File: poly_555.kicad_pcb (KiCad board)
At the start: 2 copper layers, 129 parts, among them U1 LM386, U10 555, U11 555, U12 555, U13 555, U14 555, U2 555, U3 555, U4 555, U5 555, U6 555, U7 555, U8 555, U9 555

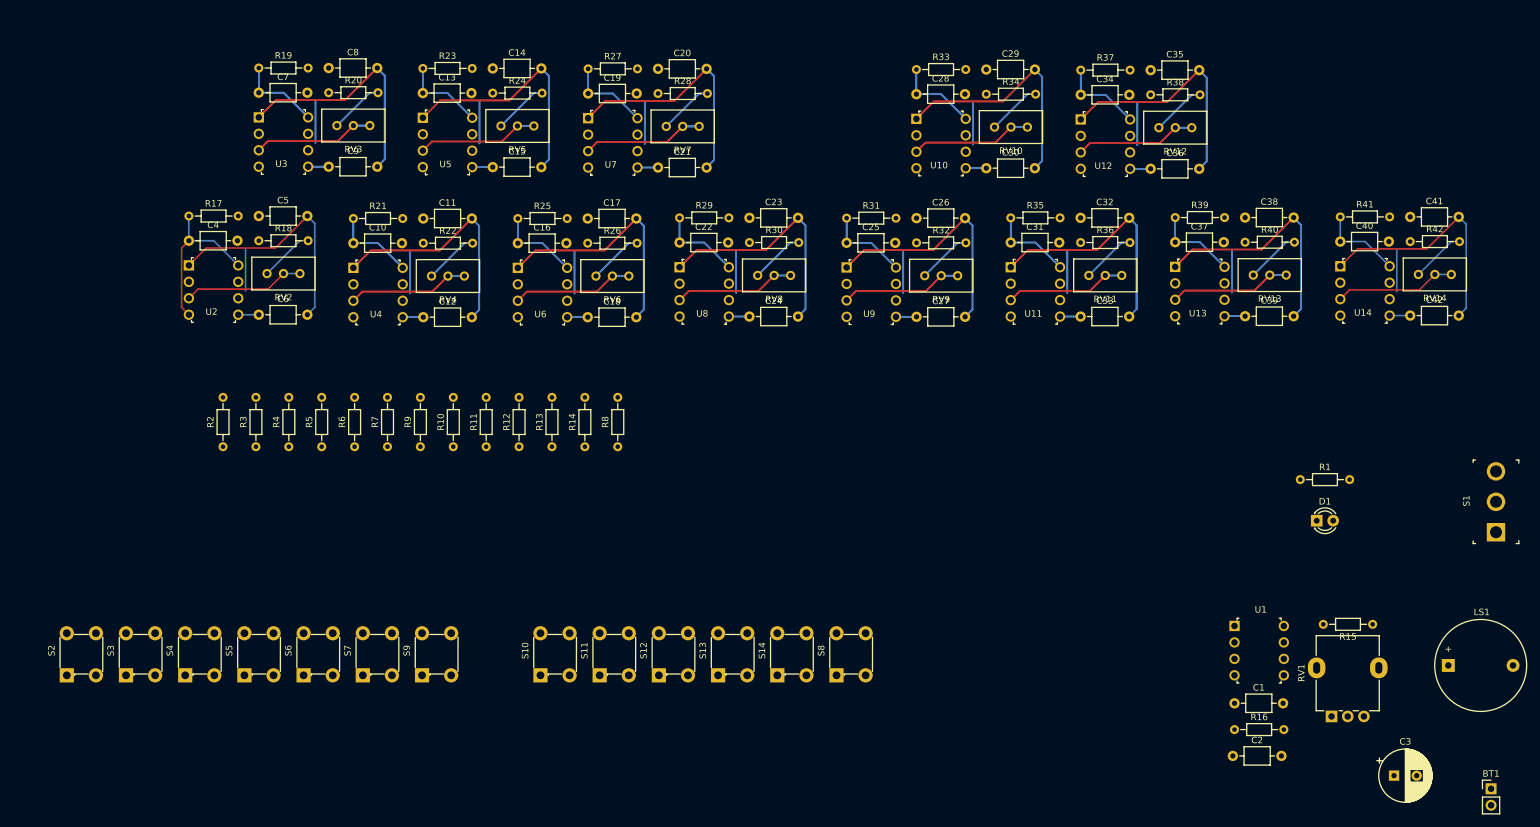
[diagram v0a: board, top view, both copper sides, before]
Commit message: Fixed button layout
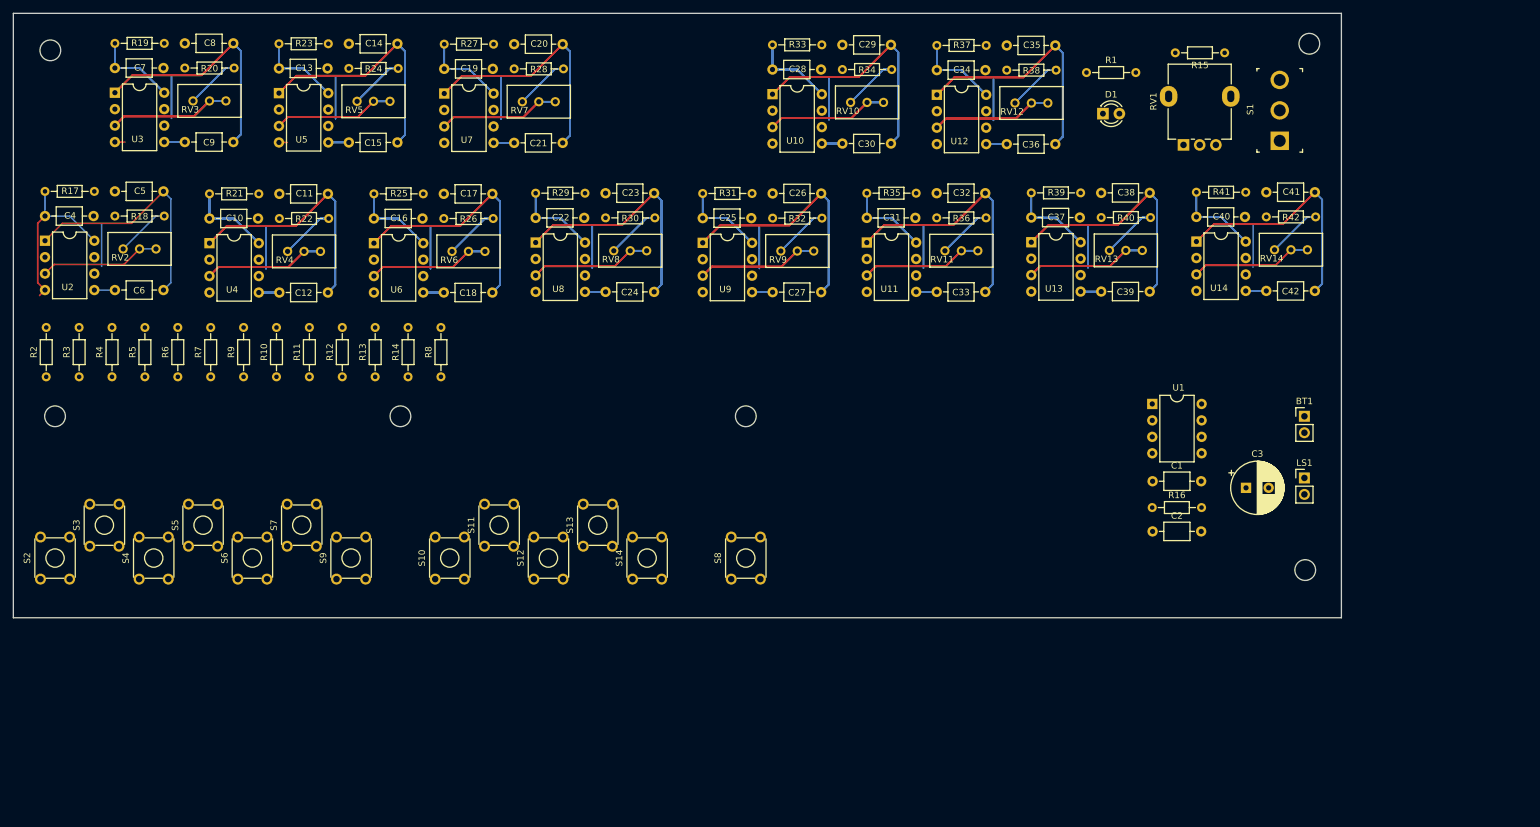
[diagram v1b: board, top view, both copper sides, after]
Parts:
- added ?: , , F.Cu at (120.4, 121.8)
- added REF**: MountingHole_3.2mm_M3, MountingHole:MountingHole_3.2mm_M3, F.Cu at (216.7, 114.6)
- added REF**: MountingHole_3.2mm_M3, MountingHole:MountingHole_3.2mm_M3, F.Cu at (217.3, 33.3)
- added REF**: MountingHole_3.2mm_M3, MountingHole:MountingHole_3.2mm_M3, F.Cu at (22.9, 34.3)
- added REF**: MountingHole_3.2mm_M3, MountingHole:MountingHole_3.2mm_M3, F.Cu at (76.9, 90.8)
- added REF**: MountingHole_3.2mm_M3, MountingHole:MountingHole_3.2mm_M3, F.Cu at (130.3, 90.8)
- added REF**: MountingHole_3.2mm_M3, MountingHole:MountingHole_3.2mm_M3, F.Cu at (23.6, 90.8)
- LS1: footprint Buzzer_Beeper:Buzzer_D14mm_H7mm_P10mm -> Connector_PinHeader_2.54mm:PinHeader_1x02_P2.54mm_Vertical
- S10, S11, S12, S13, S14, S2, S3, S4, S5, S6, S7, S8, S9: footprint digikey-footprints:Switch_Tactile_THT_6x6mm -> Button_Switch_THT:SW_TH_Tactile_Omron_B3F-10xx
- U1, U10, U11, U12, U13, U14, U2, U3, U4, U5, U6, U7, U8, U9: footprint digikey-footprints:DIP-8_W7.62mm -> Package_DIP:DIP-8_W7.62mm
- moved R15 91.2 mm to (204.2, 34.7)
- moved RV1 91.2 mm to (197.9, 48.9)
- moved D1 71.0 mm to (185.4, 44.1)
- moved R1 71.0 mm to (182.9, 37.7)
- moved S1 69.1 mm to (212.7, 48.3)
- moved BT1 64.4 mm to (216.5, 90.8)
- moved C3 50.0 mm to (207.5, 101.9)
- moved C2 36.8 mm to (193.1, 108.6)
- moved R16 36.6 mm to (193.0, 104.9)
- moved U1 36.6 mm to (193.0, 88.9)
- moved C1 36.5 mm to (193.1, 100.8)
- moved LS1 36.5 mm to (216.5, 100.3)
- moved R10 29.4 mm to (57.8, 84.7)
- moved R12 29.4 mm to (67.9, 84.7)
- moved R7 29.4 mm to (47.6, 84.7)
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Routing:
- net GND: track 903.4 -> 1355.0 mm
- net /sheet5EF60553/Out: track 37.4 -> 56.2 mm
- net /sheet5EF60554/Out: track 37.4 -> 56.2 mm
- net /sheet5EF60555/Out: track 37.4 -> 56.2 mm
- net /sheet5EF60550/Out: track 37.4 -> 56.2 mm
- net /sheet5EF27E47/Out: track 37.4 -> 56.2 mm
- net /sheet5EF259DC/Out: track 37.4 -> 56.2 mm
- net /sheet5EF7A07A/Out: track 18.7 -> 37.4 mm
- net /sheet5EF60552/Out: track 37.4 -> 56.2 mm
- net /sheet5EF17814/Out: track 37.4 -> 56.2 mm
- net /sheet5EF2B20E/Out: track 37.4 -> 56.2 mm
- net /sheet5EF2302B/Out: track 37.4 -> 56.2 mm
- net /sheet5EF60551/Out: track 37.4 -> 56.2 mm
- net /sheet5EF17814/9v: track 26.0 -> 40.6 mm
- net /sheet5EF259DC/9v: track 26.0 -> 40.3 mm
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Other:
- board outline added: 205.1 x 93.3 mm

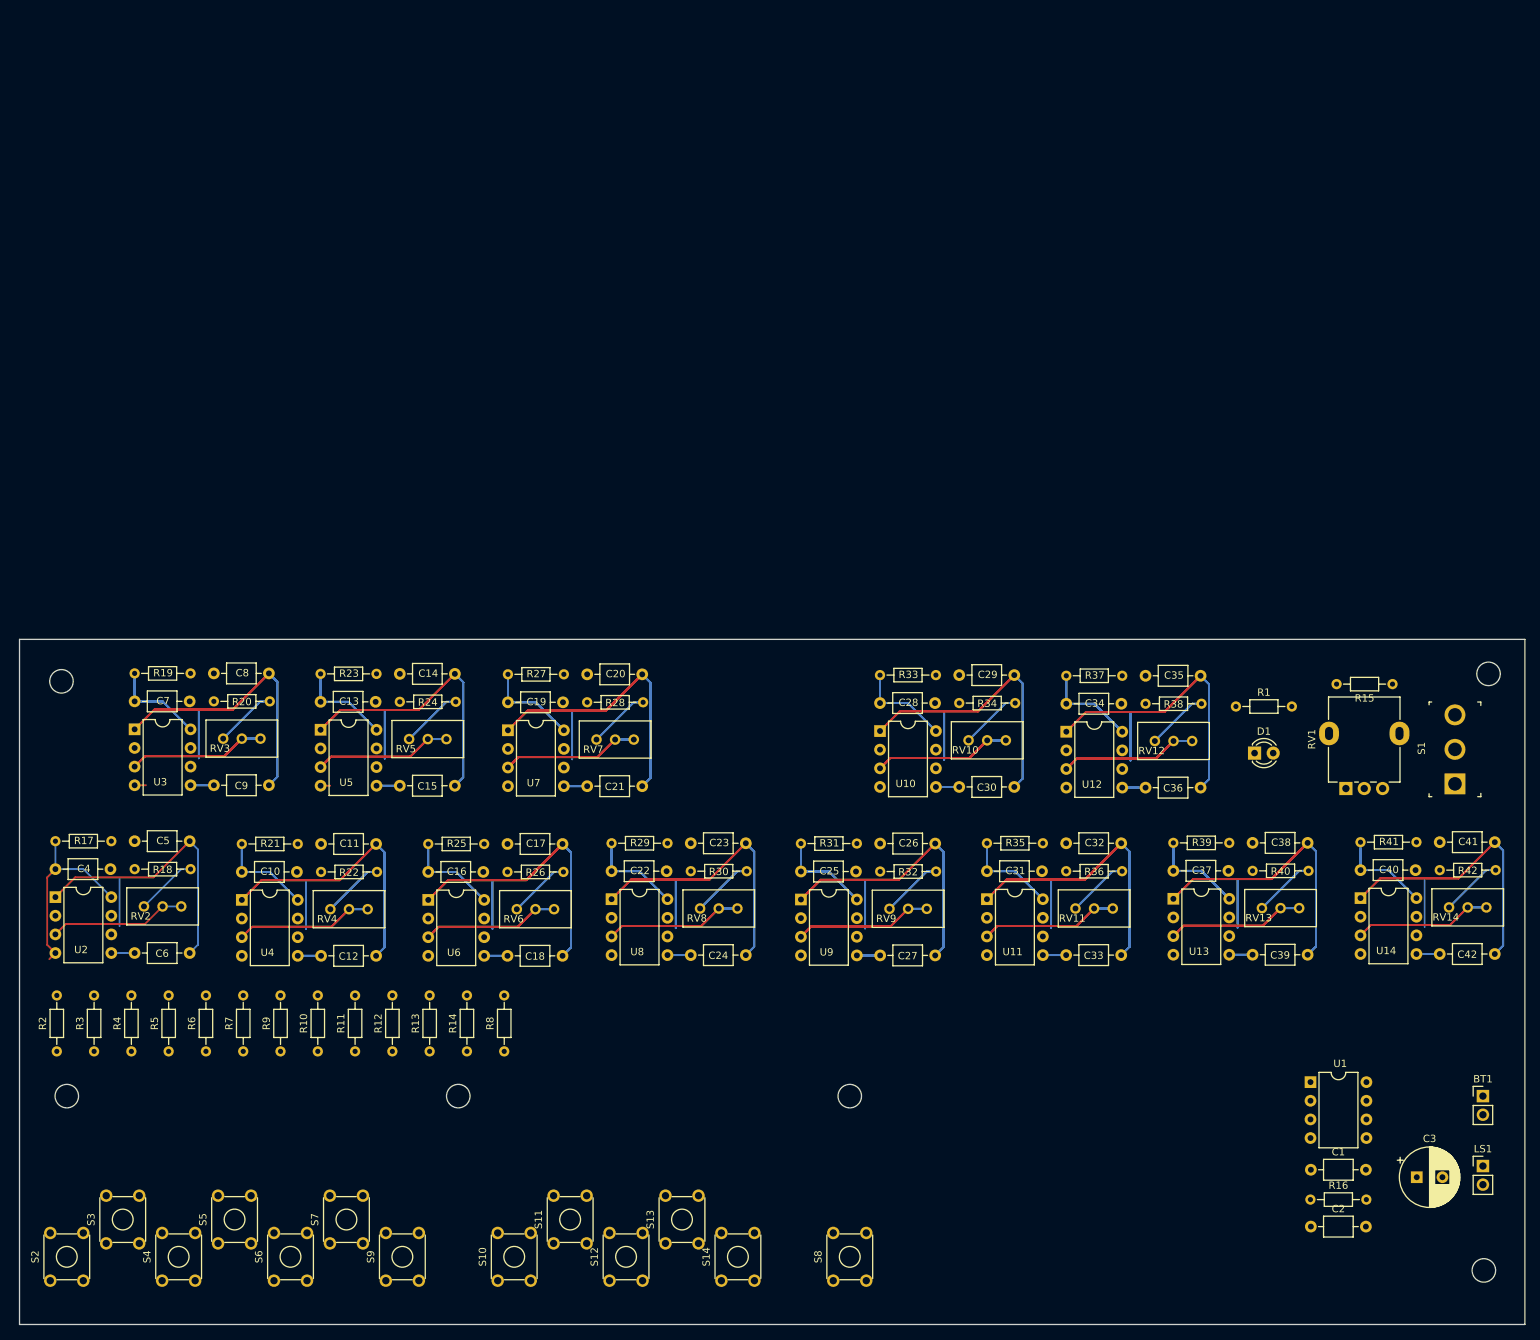
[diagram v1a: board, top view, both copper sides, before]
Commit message: Portrait layout, LEDs
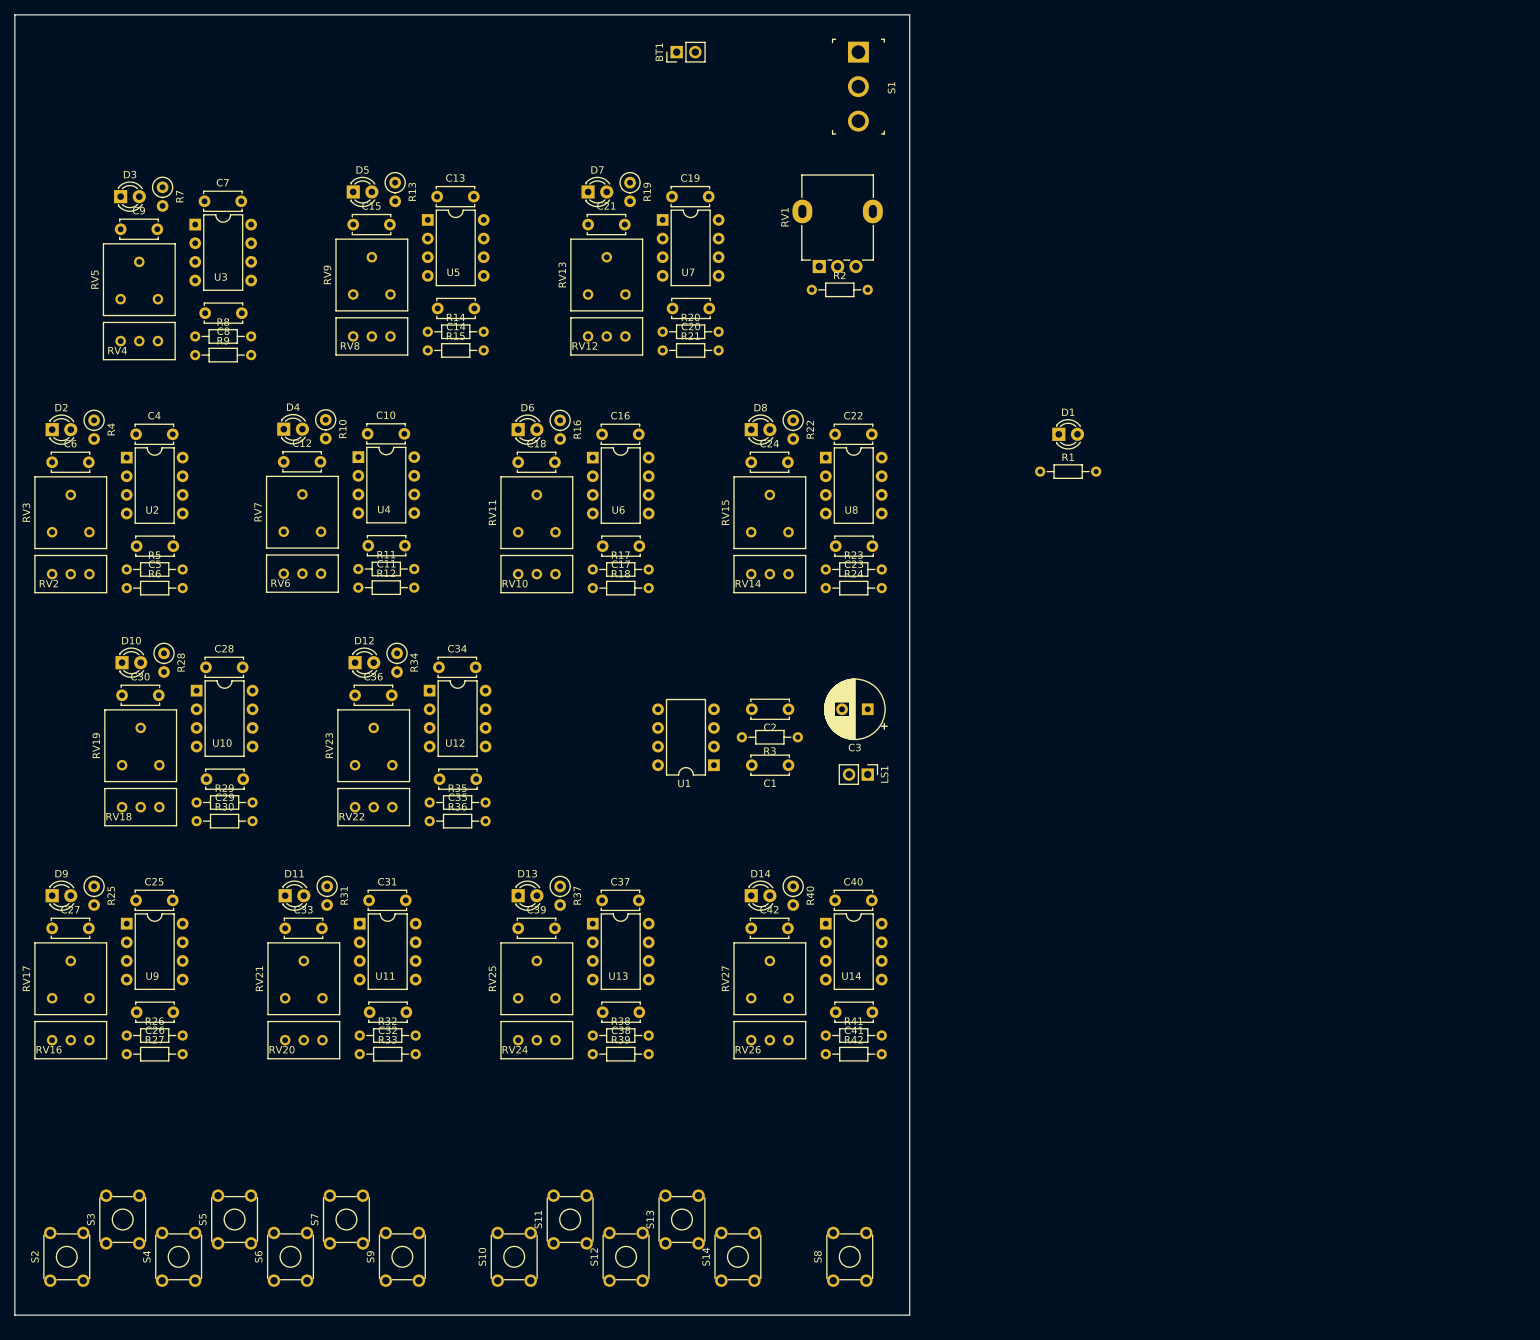
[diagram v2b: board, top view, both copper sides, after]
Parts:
- removed ?: , 
- removed REF** (x6): MountingHole_3.2mm_M3, MountingHole:MountingHole_3.2mm_M3
- added D10: LED, LED_THT:LED_D3.0mm, F.Cu at (31.1, 31.8)
- added D11: LED, LED_THT:LED_D3.0mm, F.Cu at (53.3, 63.5)
- added D12: LED, LED_THT:LED_D3.0mm, F.Cu at (62.9, 31.8)
- added D13: LED, LED_THT:LED_D3.0mm, F.Cu at (85.1, 63.5)
- added D14: LED, LED_THT:LED_D3.0mm, F.Cu at (116.8, 63.5)
- added D2: LED, LED_THT:LED_D3.0mm, F.Cu at (21.6, 0.00)
- added D3: LED, LED_THT:LED_D3.0mm, F.Cu at (30.9, -31.8)
- added D4: LED, LED_THT:LED_D3.0mm, F.Cu at (53.1, -0.06)
- added D5: LED, LED_THT:LED_D3.0mm, F.Cu at (62.6, -32.4)
- added D6: LED, LED_THT:LED_D3.0mm, F.Cu at (85.1, 0.00)
- added D7: LED, LED_THT:LED_D3.0mm, F.Cu at (94.6, -32.4)
- added D8: LED, LED_THT:LED_D3.0mm, F.Cu at (116.8, 0.00)
- added D9: LED, LED_THT:LED_D3.0mm, F.Cu at (21.6, 63.5)
- added RV15: R_POT_TRIM_US, Potentiometer_THT:Potentiometer_Bourns_3386F_Vertical, F.Cu at (121.9, 14.0)
- added RV16: R_POT_TRIM_US, Potentiometer_THT:Potentiometer_Bourns_3296W_Vertical, F.Cu at (21.6, 83.2)
- added RV17: R_POT_TRIM_US, Potentiometer_THT:Potentiometer_Bourns_3386F_Vertical, F.Cu at (26.7, 77.5)
- added RV18: R_POT_TRIM_US, Potentiometer_THT:Potentiometer_Bourns_3296W_Vertical, F.Cu at (31.1, 51.4)
- added RV19: R_POT_TRIM_US, Potentiometer_THT:Potentiometer_Bourns_3386F_Vertical, F.Cu at (36.2, 45.7)
- added RV20: R_POT_TRIM_US, Potentiometer_THT:Potentiometer_Bourns_3296W_Vertical, F.Cu at (53.3, 83.2)
- added RV21: R_POT_TRIM_US, Potentiometer_THT:Potentiometer_Bourns_3386F_Vertical, F.Cu at (58.4, 77.5)
- added RV22: R_POT_TRIM_US, Potentiometer_THT:Potentiometer_Bourns_3296W_Vertical, F.Cu at (62.9, 51.4)
- added RV23: R_POT_TRIM_US, Potentiometer_THT:Potentiometer_Bourns_3386F_Vertical, F.Cu at (67.9, 45.7)
- added RV24: R_POT_TRIM_US, Potentiometer_THT:Potentiometer_Bourns_3296W_Vertical, F.Cu at (85.1, 83.2)
- added RV25: R_POT_TRIM_US, Potentiometer_THT:Potentiometer_Bourns_3386F_Vertical, F.Cu at (90.2, 77.5)
- added RV26: R_POT_TRIM_US, Potentiometer_THT:Potentiometer_Bourns_3296W_Vertical, F.Cu at (116.8, 83.2)
- added RV27: R_POT_TRIM_US, Potentiometer_THT:Potentiometer_Bourns_3386F_Vertical, F.Cu at (121.9, 77.5)
- C1, C10, C11, C12, C13, C14, C15, C16, C17, C18, C19, C2, C20, C21, C22, C23, C24, C25, C26, C27, C28, C29, C30, C31, C32, C33, C34, C35, C36, C37, C38, C39, C4, C40, C41, C42, C5, C6, C7, C8, C9: footprint Capacitor_THT:C_Axial_L3.8mm_D2.6mm_P7.50mm_Horizontal -> Capacitor_THT:C_Disc_D5.0mm_W2.5mm_P5.00mm
- R10, R13, R4, R7: value 10k -> 330; footprint Resistor_THT:R_Axial_DIN0204_L3.6mm_D1.6mm_P7.62mm_Horizontal -> Resistor_THT:R_Axial_DIN0207_L6.3mm_D2.5mm_P2.54mm_Vertical
- R11, R14, R5, R8: value 10k -> 100k
- R15: value 10 -> 10k
- R16: value 10 -> 330; footprint Resistor_THT:R_Axial_DIN0204_L3.6mm_D1.6mm_P7.62mm_Horizontal -> Resistor_THT:R_Axial_DIN0207_L6.3mm_D2.5mm_P2.54mm_Vertical
- R18, R21, R24, R27, R30, R33, R36, R39, R42: value 100k -> 10k
- R19, R22, R25, R28, R31, R34, R37, R40: value 100k -> 330; footprint Resistor_THT:R_Axial_DIN0204_L3.6mm_D1.6mm_P7.62mm_Horizontal -> Resistor_THT:R_Axial_DIN0207_L6.3mm_D2.5mm_P2.54mm_Vertical
- R2, R3: value 10k -> 10
- RV11, RV13, RV3, RV5, RV7, RV9: footprint Potentiometer_THT:Potentiometer_Bourns_3296W_Vertical -> Potentiometer_THT:Potentiometer_Bourns_3386F_Vertical
- moved BT1 179.7 mm to (106.7, -51.4), turned to 90 degrees
- moved R16 147.4 mm to (90.8, -1.27), turned to 270 degrees
- moved R2 146.1 mm to (125.1, -19.1), turned to 0 degrees
- moved R15 139.1 mm to (72.8, -10.8), turned to 0 degrees
- moved S1 128.6 mm to (131.4, -51.4), turned to 270 degrees
- moved RV13 120.5 mm to (99.7, -18.4), turned to 90 degrees
- moved R13 118.5 mm to (68.3, -33.7), turned to 270 degrees
- moved R7 118.2 mm to (36.6, -33.0), turned to 270 degrees
- moved C30 114.7 mm to (31.1, 36.2)
- moved C27 112.9 mm to (21.6, 67.9)
- moved C36 108.4 mm to (62.9, 36.2)
- moved RV9 107.8 mm to (67.7, -18.4), turned to 90 degrees
- moved C33 106.5 mm to (53.3, 67.9)
- moved R8 106.1 mm to (41.1, -12.7), turned to 0 degrees
- moved RV14 105.4 mm to (116.8, 19.7)
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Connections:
- R10 pad 1: Net-(R10-Pad1) -> /sheet5EF2302B/9v
- R10 pad 2: /sheet5EF60551/Out -> Net-(D4-Pad2)
- R11 pad 1: Net-(R10-Pad1) -> /sheet5EF2302B/9v
- R11 pad 2: /sheet5EF60552/Out -> Net-(C11-Pad1)
- R12 pad 1: Net-(R10-Pad1) -> /555_astable/Out
- R12 pad 2: /sheet5EF60553/Out -> Net-(R12-Pad2)
- R13 pad 1: Net-(R10-Pad1) -> /sheet5EF259DC/9v
- R13 pad 2: /sheet5EF60554/Out -> Net-(D5-Pad2)
- R14 pad 1: Net-(R10-Pad1) -> /sheet5EF259DC/9v
- R14 pad 2: /sheet5EF60555/Out -> Net-(C14-Pad1)
- R15 pad 1: Net-(R15-Pad1) -> /555_astable/Out
- R15 pad 2: GND -> Net-(R15-Pad2)
- R16 pad 1: Net-(C3-Pad1) -> /sheet5EF27E47/9v
- R16 pad 2: Net-(C2-Pad1) -> Net-(D6-Pad2)
- R17 pad 1: /555_astable/9v -> /sheet5EF27E47/9v
- R17 pad 2: Net-(C5-Pad1) -> Net-(C17-Pad1)
- R18 pad 1: GND -> /555_astable/Out
- R19 pad 1: /sheet5EF17814/9v -> /sheet5EF2B20E/9v
- R19 pad 2: Net-(C8-Pad1) -> Net-(D7-Pad2)
- R2 pad 1: Net-(R10-Pad1) -> Net-(R2-Pad1)
- R2 pad 2: /555_astable/Out -> GND
- R20 pad 1: GND -> /sheet5EF2B20E/9v
- R20 pad 2: Net-(R20-Pad2) -> Net-(C20-Pad1)
- R21 pad 1: /sheet5EF2302B/9v -> /555_astable/Out
- R21 pad 2: Net-(C11-Pad1) -> Net-(R21-Pad2)
- R22 pad 1: GND -> /sheet5EF60550/9v
- R22 pad 2: Net-(R22-Pad2) -> Net-(D8-Pad2)
- R23 pad 1: /sheet5EF259DC/9v -> /sheet5EF60550/9v
- R23 pad 2: Net-(C14-Pad1) -> Net-(C23-Pad1)
- R24 pad 1: GND -> /555_astable/Out
- R25 pad 1: /sheet5EF27E47/9v -> /sheet5EF60551/9v
- R25 pad 2: Net-(C17-Pad1) -> Net-(D9-Pad2)
- R26 pad 1: GND -> /sheet5EF60551/9v
- R26 pad 2: Net-(R26-Pad2) -> Net-(C26-Pad1)
- R27 pad 1: /sheet5EF2B20E/9v -> /555_astable/Out
- R27 pad 2: Net-(C20-Pad1) -> Net-(R27-Pad2)
- R28 pad 1: GND -> /sheet5EF60552/9v
- R28 pad 2: Net-(R28-Pad2) -> Net-(D10-Pad2)
- R29 pad 1: /sheet5EF60550/9v -> /sheet5EF60552/9v
- R29 pad 2: Net-(C23-Pad1) -> Net-(C29-Pad1)
- R3 pad 1: Net-(R10-Pad1) -> Net-(C3-Pad1)
- R3 pad 2: /sheet5EF17814/Out -> Net-(C2-Pad1)
- R30 pad 1: GND -> /555_astable/Out
- R31 pad 1: /sheet5EF60551/9v -> /sheet5EF60553/9v
- R31 pad 2: Net-(C26-Pad1) -> Net-(D11-Pad2)
- R32 pad 1: GND -> /sheet5EF60553/9v
- R32 pad 2: Net-(R32-Pad2) -> Net-(C32-Pad1)
- R33 pad 1: /sheet5EF60552/9v -> /555_astable/Out
- R33 pad 2: Net-(C29-Pad1) -> Net-(R33-Pad2)
- R34 pad 1: GND -> /sheet5EF60554/9v
- R34 pad 2: Net-(R34-Pad2) -> Net-(D12-Pad2)
- R35 pad 1: /sheet5EF60553/9v -> /sheet5EF60554/9v
- R35 pad 2: Net-(C32-Pad1) -> Net-(C35-Pad1)
- R36 pad 1: GND -> /555_astable/Out
- R37 pad 1: /sheet5EF60554/9v -> /sheet5EF60555/9v
- R37 pad 2: Net-(C35-Pad1) -> Net-(D13-Pad2)
- R38 pad 1: GND -> /sheet5EF60555/9v
- R38 pad 2: Net-(R38-Pad2) -> Net-(C38-Pad1)
- R39 pad 1: /sheet5EF60555/9v -> /555_astable/Out
- R39 pad 2: Net-(C38-Pad1) -> Net-(R39-Pad2)
- R4 pad 1: Net-(R10-Pad1) -> /555_astable/9v
- R4 pad 2: /sheet5EF2302B/Out -> Net-(D2-Pad2)
- R40 pad 1: GND -> /sheet5EF7A07A/9v
- R40 pad 2: Net-(R40-Pad2) -> Net-(D14-Pad2)
- R42 pad 1: GND -> /555_astable/Out
- R5 pad 1: Net-(R10-Pad1) -> /555_astable/9v
- R5 pad 2: /sheet5EF259DC/Out -> Net-(C5-Pad1)
- R6 pad 1: Net-(R10-Pad1) -> /555_astable/Out
- R6 pad 2: /sheet5EF27E47/Out -> Net-(R6-Pad2)
- R7 pad 1: Net-(R10-Pad1) -> /sheet5EF17814/9v
- R7 pad 2: /sheet5EF2B20E/Out -> Net-(D3-Pad2)
- R8 pad 1: Net-(R10-Pad1) -> /sheet5EF17814/9v
- R8 pad 2: /sheet5EF7A07A/Out -> Net-(C8-Pad1)
- R9 pad 1: Net-(R10-Pad1) -> /555_astable/Out
- R9 pad 2: /sheet5EF60550/Out -> Net-(R9-Pad2)
- RV1 pad 2: Net-(R15-Pad1) -> Net-(R2-Pad1)
- RV1 pad 3: Net-(R10-Pad1) -> /555_astable/Out
- RV10 pad 1: Net-(R34-Pad2) -> GND
- RV10 pad 2: /sheet5EF60552/Out -> Net-(RV10-Pad2)
- RV10 pad 3: /sheet5EF60552/Out -> Net-(RV10-Pad2)
- RV11 pad 1: Net-(R36-Pad2) -> Net-(RV10-Pad2)
- RV11 pad 2: /sheet5EF60553/Out -> Net-(R18-Pad2)
- RV11 pad 3: /sheet5EF60553/Out -> Net-(R18-Pad2)
- RV12 pad 1: Net-(R38-Pad2) -> GND
- RV12 pad 2: /sheet5EF60554/Out -> Net-(RV12-Pad2)
- RV12 pad 3: /sheet5EF60554/Out -> Net-(RV12-Pad2)
- RV13 pad 1: Net-(R40-Pad2) -> Net-(RV12-Pad2)
- RV13 pad 2: /sheet5EF60555/Out -> Net-(R21-Pad2)
- RV13 pad 3: /sheet5EF60555/Out -> Net-(R21-Pad2)
- RV14 pad 1: Net-(R42-Pad2) -> GND
- RV14 pad 2: /sheet5EF7A07A/Out -> Net-(RV14-Pad2)
- RV14 pad 3: /sheet5EF7A07A/Out -> Net-(RV14-Pad2)
- RV2 pad 1: Net-(R18-Pad2) -> GND
- RV2 pad 2: /555_astable/Out -> Net-(RV2-Pad2)
- RV2 pad 3: /555_astable/Out -> Net-(RV2-Pad2)
- RV3 pad 1: Net-(R20-Pad2) -> Net-(RV2-Pad2)
- RV3 pad 2: /sheet5EF17814/Out -> Net-(R6-Pad2)
- RV3 pad 3: /sheet5EF17814/Out -> Net-(R6-Pad2)
- RV4 pad 1: Net-(R22-Pad2) -> GND
- RV4 pad 2: /sheet5EF2302B/Out -> Net-(RV4-Pad2)
- RV4 pad 3: /sheet5EF2302B/Out -> Net-(RV4-Pad2)
- RV5 pad 1: Net-(R24-Pad2) -> Net-(RV4-Pad2)
- RV5 pad 2: /sheet5EF259DC/Out -> Net-(R9-Pad2)
- RV5 pad 3: /sheet5EF259DC/Out -> Net-(R9-Pad2)
- RV6 pad 1: Net-(R26-Pad2) -> GND
- RV6 pad 2: /sheet5EF27E47/Out -> Net-(RV6-Pad2)
- RV6 pad 3: /sheet5EF27E47/Out -> Net-(RV6-Pad2)
- RV7 pad 1: Net-(R28-Pad2) -> Net-(RV6-Pad2)
- RV7 pad 2: /sheet5EF2B20E/Out -> Net-(R12-Pad2)
- RV7 pad 3: /sheet5EF2B20E/Out -> Net-(R12-Pad2)
- RV8 pad 1: Net-(R30-Pad2) -> GND
- RV8 pad 2: /sheet5EF60550/Out -> Net-(RV8-Pad2)
- RV8 pad 3: /sheet5EF60550/Out -> Net-(RV8-Pad2)
- RV9 pad 1: Net-(R32-Pad2) -> Net-(RV8-Pad2)
- RV9 pad 2: /sheet5EF60551/Out -> Net-(R15-Pad2)
- RV9 pad 3: /sheet5EF60551/Out -> Net-(R15-Pad2)
- U1 pad 2: Net-(R15-Pad1) -> Net-(R2-Pad1)
- U10 pad 3: /sheet5EF60552/Out -> Net-(R30-Pad2)
- U11 pad 3: /sheet5EF60553/Out -> Net-(R33-Pad2)
- U12 pad 3: /sheet5EF60554/Out -> Net-(R36-Pad2)
- U13 pad 3: /sheet5EF60555/Out -> Net-(R39-Pad2)
- U14 pad 3: /sheet5EF7A07A/Out -> Net-(R42-Pad2)
- U2 pad 3: /555_astable/Out -> Net-(R6-Pad2)
- U3 pad 3: /sheet5EF17814/Out -> Net-(R9-Pad2)
- U4 pad 3: /sheet5EF2302B/Out -> Net-(R12-Pad2)
- U5 pad 3: /sheet5EF259DC/Out -> Net-(R15-Pad2)
- U6 pad 3: /sheet5EF27E47/Out -> Net-(R18-Pad2)
- U7 pad 3: /sheet5EF2B20E/Out -> Net-(R21-Pad2)
- U8 pad 3: /sheet5EF60550/Out -> Net-(R24-Pad2)
- U9 pad 3: /sheet5EF60551/Out -> Net-(R27-Pad2)
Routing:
- net GND: track 1355.0 -> 0.00 mm
- net /555_astable/Gnd: track 156.5 -> 0.00 mm
- net /sheet5EF60555/Out: track 56.2 -> 0.00 mm
- net /sheet5EF60554/Out: track 56.2 -> 0.00 mm
- net /sheet5EF60553/Out: track 56.2 -> 0.00 mm
- net /sheet5EF259DC/Out: track 56.2 -> 0.00 mm
- net /sheet5EF27E47/Out: track 56.2 -> 0.00 mm
- net /sheet5EF2302B/Out: track 56.2 -> 0.00 mm
- net /sheet5EF17814/Out: track 56.2 -> 0.00 mm
- net /sheet5EF60550/Out: track 56.2 -> 0.00 mm
- net /sheet5EF2B20E/Out: track 56.2 -> 0.00 mm
- net /sheet5EF60552/Out: track 56.2 -> 0.00 mm
- net /sheet5EF60551/Out: track 56.2 -> 0.00 mm
- net /sheet5EF17814/9v: track 40.6 -> 0.00 mm
- net /sheet5EF259DC/9v: track 40.3 -> 0.00 mm
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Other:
- board size 205.1 x 93.3 mm -> 121.9 x 177.2 mm
